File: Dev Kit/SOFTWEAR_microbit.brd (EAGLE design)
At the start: 25.7 x 53.8 mm, 32 parts, among them J1 455-1750-1-ND, J4 QWIIC_RIGHT_ANGLE, J6 QWIIC_RIGHT_ANGLE, M1 MOTORSMD, Q1 500mA/300V, U5 OPA344, U6 ADMP401, U7 APDS-9960, X1 SM03B-SRSS-TB, X2 SM03B-SRSS-TB, X4 SM03B-SRSS-TB

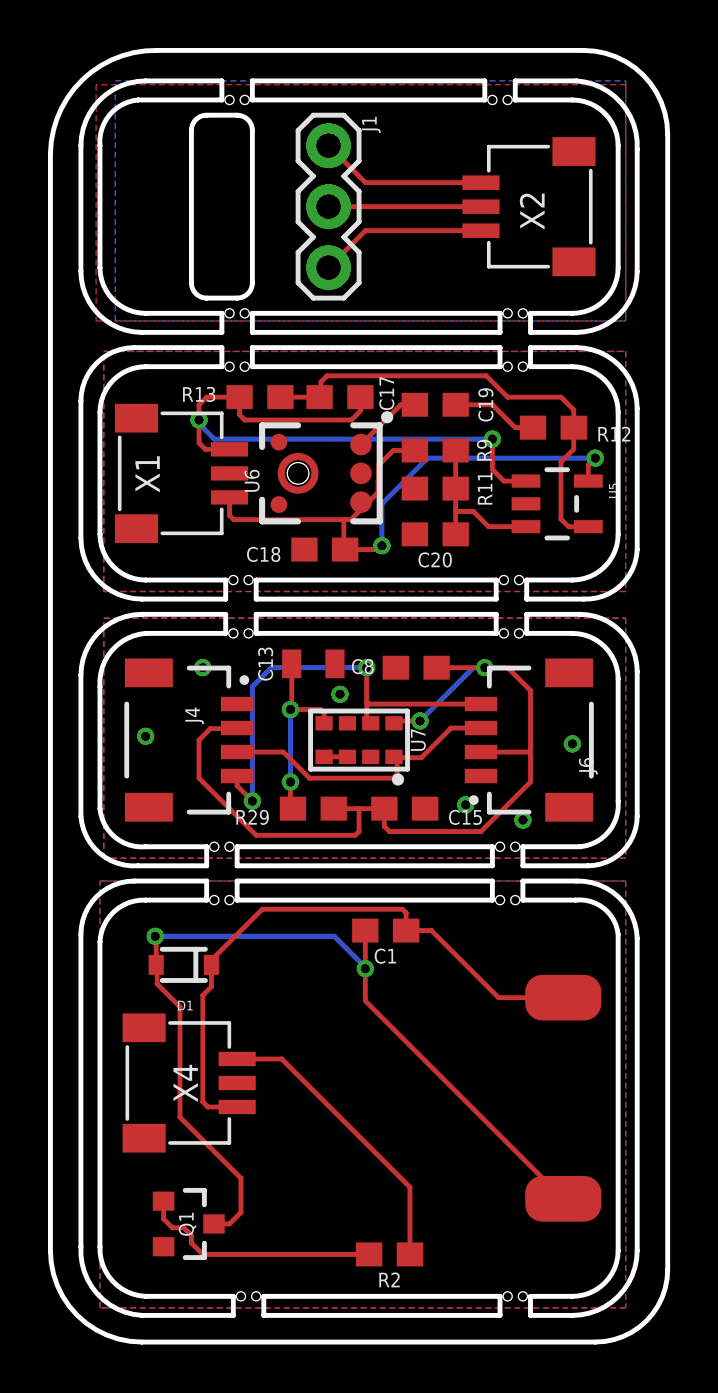
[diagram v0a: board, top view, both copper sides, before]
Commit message: added cap touch BOB
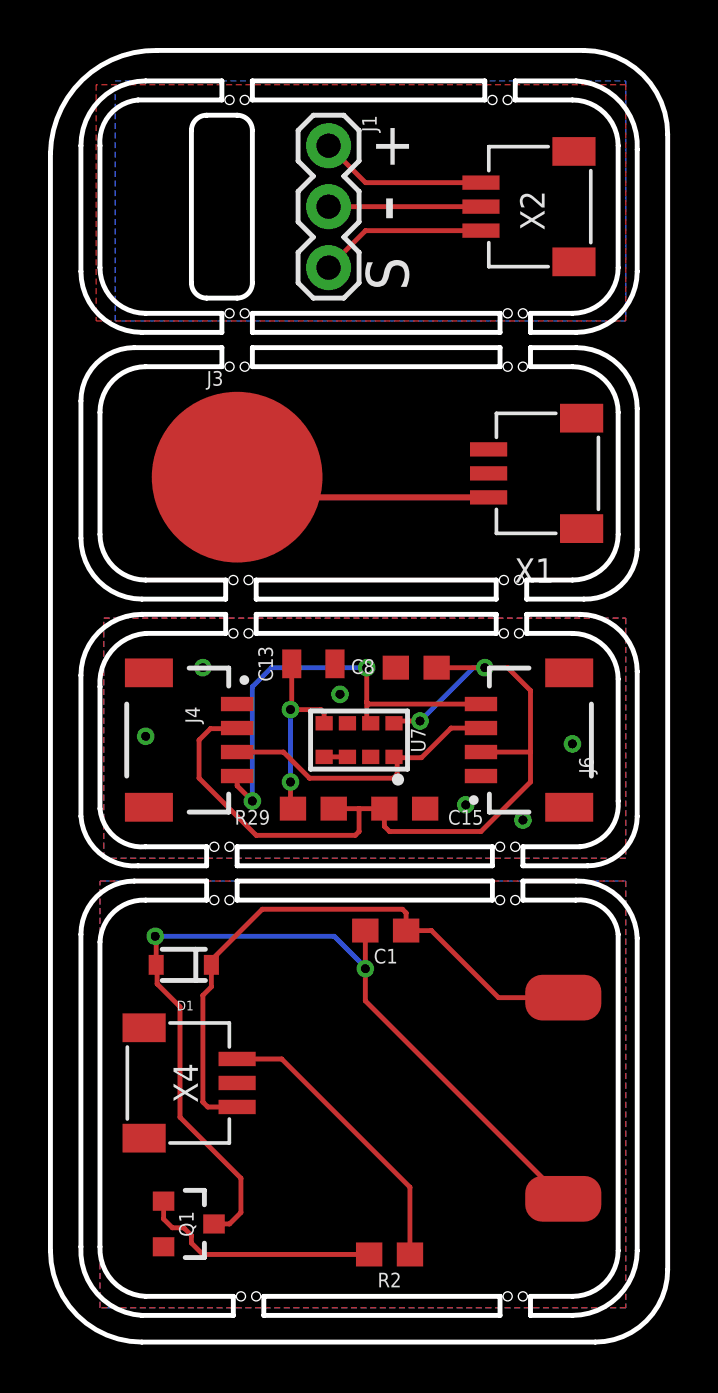
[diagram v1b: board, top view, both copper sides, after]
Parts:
- removed C17: 100pF, SparkFun-Capacitors:0603
- removed C18: 0.1uF, SparkFun-Capacitors:0603
- removed C19: 4.7uF, SparkFun-Capacitors:0603
- removed C20: 1.0uF, SparkFun-Capacitors:0603
- removed R11, R9: 10k, SparkFun-Resistors:0603
- removed R12: 1.5k, SparkFun-Resistors:0603
- removed R13: 100k, SparkFun-Resistors:0603
- removed U5: OPA344, SparkFun:SOT23-5
- removed U6: ADMP401, SparkFun-Sensors:ADMP401
- added J3: (no value), SparkFun-Connectors:SPRING-CONNECTOR
- U$1: device buzzard_labels (21):AUDIO7 -> buzzard_labels (21):SOFTWEAR#3
- moved U$1 13.7 mm to (27.9, 48.7)
- moved X1 10.8 mm to (22.9, 37.6), turned to 270 degrees
- moved U$4 1.36 mm to (22.5, 37.6)
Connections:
- removed net 3.3V: C18.2, R9.2, U5.5, U6.5, X1.3
- removed net A3: C17.2, R13.1, U5.1, X1.1
- removed net N$1: C19.1, U6.1
- removed net N$10: C19.2, R12.2
- removed net N$11: C20.1, R11.2, R9.1, U5.3
- removed net N$13: C18.1, C20.2, R11.1, U5.2, U6.2, U6.4, U6.6, X1.2
- net N$6: now also J3.P$2, X1.1; no longer C17.1, R12.1, R13.2, U5.4
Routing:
- net A3: track 26.9 -> 0.00 mm, vias 2 -> 0
- net 3.3V: track 25.9 -> 0.00 mm, vias 2 -> 0
- net N$6: track 19.6 -> 12.2 mm
- net N$11: track 6.69 -> 0.00 mm
- net N$10: track 3.62 -> 0.00 mm
- net N$1: track 2.93 -> 0.00 mm
- removed copper zone on layer 1, net N$13
- removed copper zone on layer 16, net N$13
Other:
- board text added: "+"
- board text added: "-"
- board text added: "S"
